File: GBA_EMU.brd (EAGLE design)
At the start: 130.7 x 72.9 mm, 99 parts, among them J1 USB-MINIB-5PIN, J2 AVR_SPI, SW1 LEFT, SW2 RIGHT, SW3 PWR_SWITCH, U1 MIC7221, U2 MCP1642B-ADJ, U4 LM4875, U5 Mic5365-2.8Y, U7 AZV321, X2 HEADPHONE

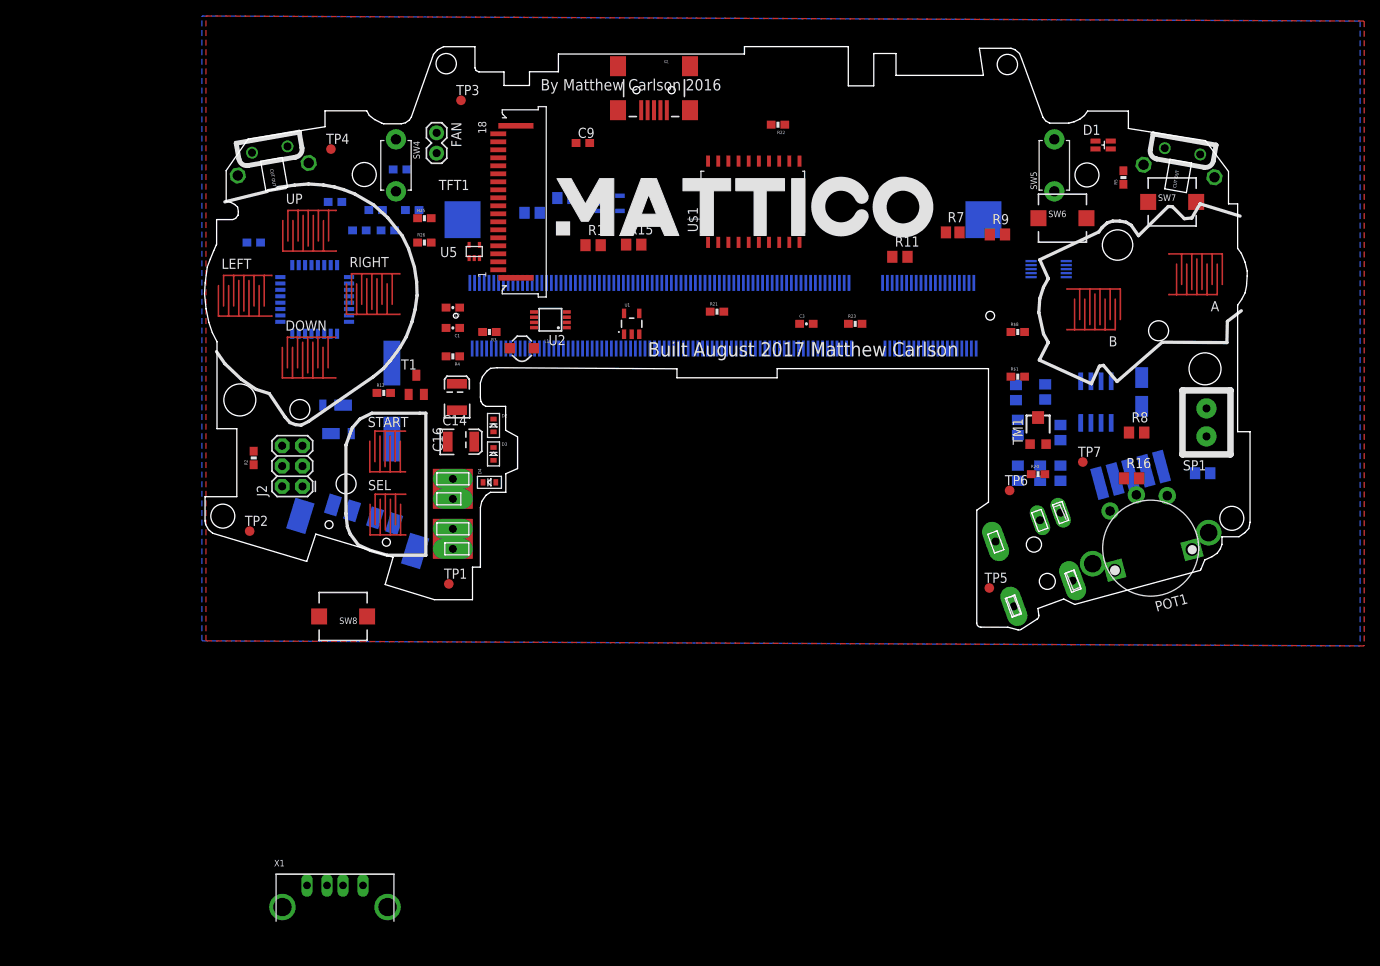
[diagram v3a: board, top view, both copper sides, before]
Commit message: moved connectors and whatnot
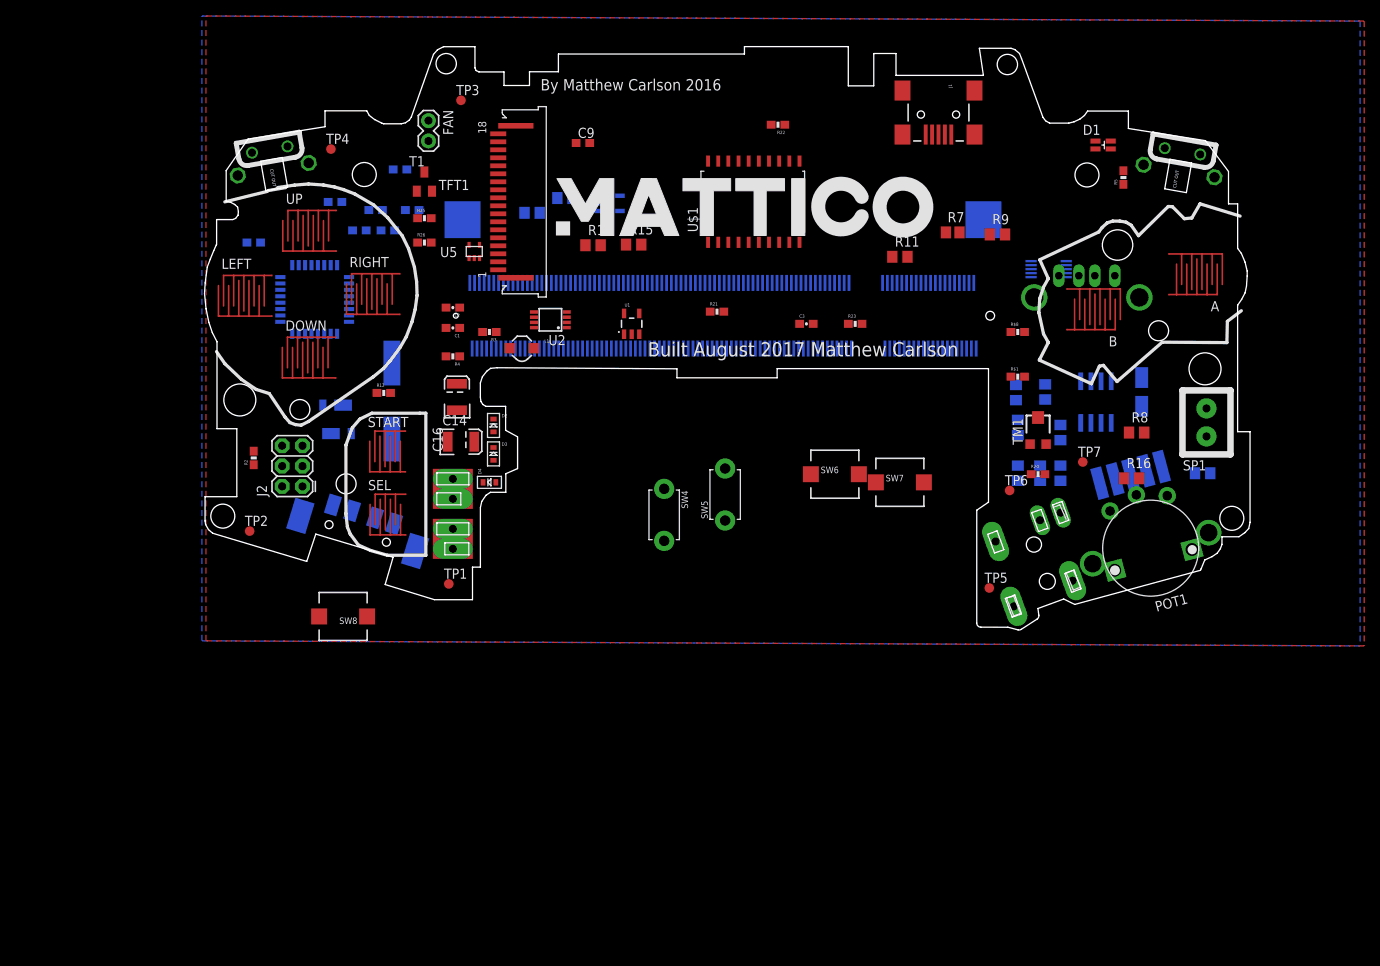
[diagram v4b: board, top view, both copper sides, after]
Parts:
- moved X1 121.0 mm to (131.6, 46.7), flipped to the bottom
- moved SW5 58.2 mm to (86.4, 25.9)
- moved SW4 55.1 mm to (78.7, 23.4)
- moved SW7 48.9 mm to (108.2, 27.4)
- moved SW6 42.8 mm to (100.1, 28.4)
- moved J1 35.7 mm to (113.0, 73.4)
- moved T1 25.4 mm to (48.8, 65.0)
- moved FAN 1.83 mm to (49.3, 72.6)
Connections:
- new net N$38: PCB1.47
- new net N$41: PCB1.23
- new net N$42: PCB1.27
- new net N$43: PCB1.29
- new net PI_SHUTDOWN: PCB1.69

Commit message: updated board render
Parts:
- moved SW5 49.9 mm to (99.1, 74.2)
- moved SW4 49.3 mm to (79.2, 72.6)
- moved SW7 21.3 mm to (112.8, 48.3)
- moved SW6 18.4 mm to (87.9, 42.2)
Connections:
- removed net N$38: PCB1.47
- net Y_BTN: now also PCB1.47
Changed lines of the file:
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@@
 <element name="U$1" library="custom" package="S020-75MM" value="CBT3244AD" x="84.224" y="62.512" rot="R90"/>
 <element name="POT1" library="adafruit" package="THUMBWHEEL" value="THUMBPOT" x="139.5508" y="19.2032" rot="R195"/>
-<element name="SW4" library="adafruit" package="TACT_PANA-EVQ" value="" x="78.74" y="23.368" rot="R270"/>
-<element name="SW5" library="adafruit" package="TACT_PANA-EVQ" value="" x="86.36" y="25.908" rot="R90"/>
+<element name="SW4" library="adafruit" package="TACT_PANA-EVQ" value="" x="79.248" y="72.644" rot="R270"/>
+<element name="SW5" library="adafruit" package="TACT_PANA-EVQ" value="" x="99.06" y="74.168" rot="R90"/>
 <element name="R13" library="SparkFun-Resistors" package="0603-RES" value="4.7K" x="45.72" y="66.548" rot="MR180">
 <attribute name="PROD_ID" value="RES-07857" x="45.72" y="66.548" size="1.778" layer="28" rot="MR180" display="off"/>
 </element>
-<element name="SW6" library="adafruit" package="PUSHBUTTON_SMD_SJ" value="" x="100.076" y="28.448"/>
-<element name="SW7" library="adafruit" package="PUSHBUTTON_SMD_SJ" value="" x="108.204" y="27.432"/>
+<element name="SW6" library="adafruit" package="PUSHBUTTON_SMD_SJ" value="" x="87.884" y="42.164"/>
+<element name="SW7" library="adafruit" package="PUSHBUTTON_SMD_SJ" value="" x="112.776" y="48.26"/>
 <element name="COPRO" library="adafruit" package="TQFP32-08" value="MEGA16u2" x="35.052" y="50.292" rot="MR0"/>
 <element name="R17" library="SparkFun-Resistors" package="0603-RES" value="22" x="37.592" y="62.484" rot="MR0">
@@
 <wire x1="106.94" y1="44.16" x2="108.74" y2="44.16" width="0" layer="19" extent="16-16"/>
 <wire x1="59.84" y1="52.36" x2="58.04" y2="52.36" width="0" layer="19" extent="16-16"/>
-<wire x1="55.64" y1="52.36" x2="58.04" y2="52.36" width="0" layer="19" extent="16-16"/>
-<wire x1="97.94" y1="44.16" x2="97.37" y2="47.244" width="0" layer="19" extent="1-16"/>
+<wire x1="85.34" y1="44.16" x2="84.884" y2="42.164" width="0" layer="19" extent="1-16"/>
+<wire x1="87.14" y1="44.16" x2="85.34" y2="44.16" width="0" layer="19" extent="16-16"/>
+<wire x1="88.94" y1="44.16" x2="87.14" y2="44.16" width="0" layer="19" extent="16-16"/>
+<wire x1="90.74" y1="44.16" x2="88.94" y2="44.16" width="0" layer="19" extent="16-16"/>
+<wire x1="92.54" y1="44.16" x2="90.74" y2="44.16" width="0" layer="19" extent="16-16"/>
+<wire x1="94.34" y1="44.16" x2="92.54" y2="44.16" width="0" layer="19" extent="16-16"/>
+<wire x1="96.14" y1="44.16" x2="94.34" y2="44.16" width="0" layer="19" extent="16-16"/>
+<wire x1="97.94" y1="44.16" x2="96.14" y2="44.16" width="0" layer="19" extent="16-16"/>
 <wire x1="99.74" y1="44.16" x2="97.94" y2="44.16" width="0" layer="19" extent="16-16"/>
 <wire x1="101.54" y1="44.16" x2="99.74" y2="44.16" width="0" layer="19" extent="16-16"/>
-<wire x1="96.14" y1="44.16" x2="97.94" y2="44.16" width="0" layer="19" extent="16-16"/>
-<wire x1="94.34" y1="44.16" x2="96.14" y2="44.16" width="0" layer="19" extent="16-16"/>
-<wire x1="92.54" y1="44.16" x2="94.34" y2="44.16" width="0" layer="19" extent="16-16"/>
-<wire x1="90.74" y1="44.16" x2="92.54" y2="44.16" width="0" layer="19" extent="16-16"/>
-<wire x1="88.94" y1="44.16" x2="90.74" y2="44.16" width="0" layer="19" extent="16-16"/>
-<wire x1="87.14" y1="44.16" x2="88.94" y2="44.16" width="0" layer="19" extent="16-16"/>
-<wire x1="85.34" y1="44.16" x2="87.14" y2="44.16" width="0" layer="19" extent="16-16"/>
 <wire x1="83.54" y1="44.16" x2="85.34" y2="44.16" width="0" layer="19" extent="16-16"/>
 <wire x1="81.74" y1="44.16" x2="83.54" y2="44.16" width="0" layer="19" extent="16-16"/>
@@
 <wire x1="65.54" y1="44.16" x2="67.34" y2="44.16" width="0" layer="19" extent="16-16"/>
 <wire x1="63.74" y1="44.16" x2="65.54" y2="44.16" width="0" layer="19" extent="16-16"/>
+<wire x1="55.64" y1="52.36" x2="58.04" y2="52.36" width="0" layer="19" extent="16-16"/>
 <wire x1="55" y1="55.46125" x2="55.64" y2="52.36" width="0" layer="19" extent="1-16"/>
 <wire x1="37.737625" y1="61.42204375" x2="39.79" y2="58.928" width="0" layer="19" extent="1-16"/>
@@
 <wire x1="52.324" y1="21.618" x2="46.42191875" y2="25.943271875" width="0" layer="19" extent="1-1"/>
 <wire x1="52.324" y1="19.118" x2="52.324" y2="21.618" width="0" layer="19" extent="1-1"/>
-<wire x1="86.36" y1="29.158" x2="87.14" y2="44.16" width="0" layer="19" extent="16-16"/>
 </signal>
 <signal name="TXD">
@@
 <contactref element="R26" pad="1"/>
 <contactref element="PCB1" pad="83"/>
-<wire x1="103.076" y1="28.448" x2="89.54" y2="44.16" width="0" layer="19" extent="1-16"/>
+<wire x1="90.884" y1="42.164" x2="89.54" y2="44.16" width="0" layer="19" extent="1-16"/>
 <wire x1="47.918" y1="57.404" x2="89.54" y2="44.16" width="0" layer="19" extent="1-16"/>
 </signal>
@@
 <contactref element="R25" pad="1"/>
 <contactref element="SW7" pad="P$1"/>
-<wire x1="47.918" y1="60.452" x2="111.204" y2="27.432" width="0" layer="19" extent="1-1"/>
+<contactref element="PCB1" pad="47"/>
+<wire x1="100.34" y1="44.16" x2="115.776" y2="48.26" width="0" layer="19" extent="1-16"/>
+<wire x1="47.918" y1="60.452" x2="100.34" y2="44.16" width="0" layer="19" extent="1-16"/>
 </signal>
 <signal name="L2_BTN">
@@
 <contactref element="SW4" pad="P$1"/>
 <contactref element="PCB1" pad="57"/>
-<wire x1="78.74" y1="26.618" x2="97.34" y2="44.16" width="0" layer="19" extent="16-16"/>
-<wire x1="27.432" y1="29.63" x2="78.74" y2="26.618" width="0" layer="19" extent="1-1"/>
+<wire x1="97.34" y1="44.16" x2="79.248" y2="75.894" width="0" layer="19" extent="16-16"/>
+<wire x1="27.432" y1="29.63" x2="79.248" y2="75.894" width="0" layer="19" extent="1-1"/>
 </signal>
 <signal name="R2_BTN">
@@
 <contactref element="SW5" pad="P$1"/>
 <contactref element="PCB1" pad="45"/>
-<wire x1="86.36" y1="22.658" x2="100.94" y2="44.16" width="0" layer="19" extent="16-16"/>
-<wire x1="44.87" y1="66.548" x2="100.94" y2="44.16" width="0" layer="19" extent="16-16"/>
+<wire x1="100.94" y1="44.16" x2="99.06" y2="70.918" width="0" layer="19" extent="16-16"/>
+<wire x1="44.87" y1="66.548" x2="99.06" y2="70.918" width="0" layer="19" extent="16-16"/>
 </signal>
 <signal name="COPRO_RX">
@@
 <contactref element="PCB1" pad="69"/>
 </signal>
-<signal name="N$38">
-<contactref element="PCB1" pad="47"/>
-</signal>
 <signal name="N$41">

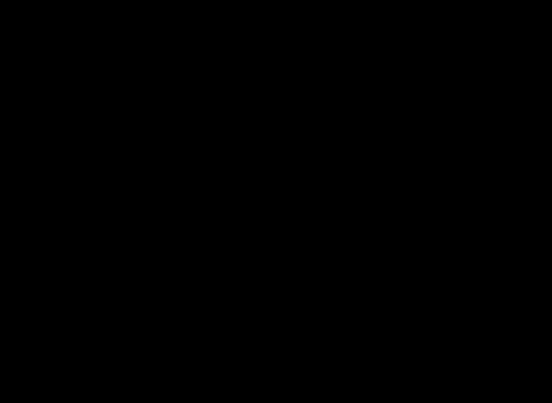
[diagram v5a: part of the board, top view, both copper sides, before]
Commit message: moved some labels around
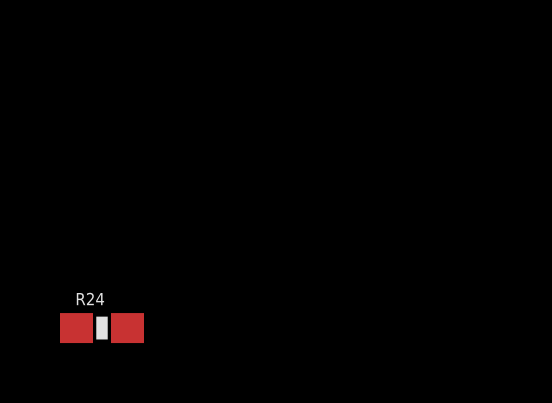
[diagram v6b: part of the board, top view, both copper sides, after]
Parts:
- added R24: 10K, SparkFun-Resistors:0603-RES
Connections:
- new net N$38: R24.2
- net PWR_EN: now also R24.1
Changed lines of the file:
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@@
 <element name="D6" library="custom" package="DIODE_POWERDI_123" value="" x="37.084" y="33.528" rot="MR180"/>
 <element name="X1" library="Adafruit_PowerBoost" package="MICROBUILDER_USB_HOST-PTH" value="" x="131.572" y="46.736" rot="MR0"/>
+<element name="R24" library="SparkFun-Resistors" package="0603-RES" value="10K" x="17.272" y="-10.16">
+<attribute name="PROD_ID" value="RES-00824" x="17.272" y="-10.16" size="1.778" layer="27" display="off"/>
+</element>
 </elements>
 <signals>
@@
 <contactref element="U2" pad="1"/>
 <contactref element="COPRO" pad="6"/>
+<contactref element="R24" pad="1"/>
 <wire x1="39.3446" y1="49.092" x2="66.566" y2="46.777" width="0" layer="19" extent="1-16"/>
+<wire x1="16.422" y1="-10.16" x2="39.3446" y2="49.092" width="0" layer="19" extent="1-16"/>
 </signal>
 <signal name="PI_SHUTDOWN">
@@
 <contactref element="PCB1" pad="29"/>
 </signal>
+<signal name="N$38">
+<contactref element="R24" pad="2"/>
+</signal>
 </signals>

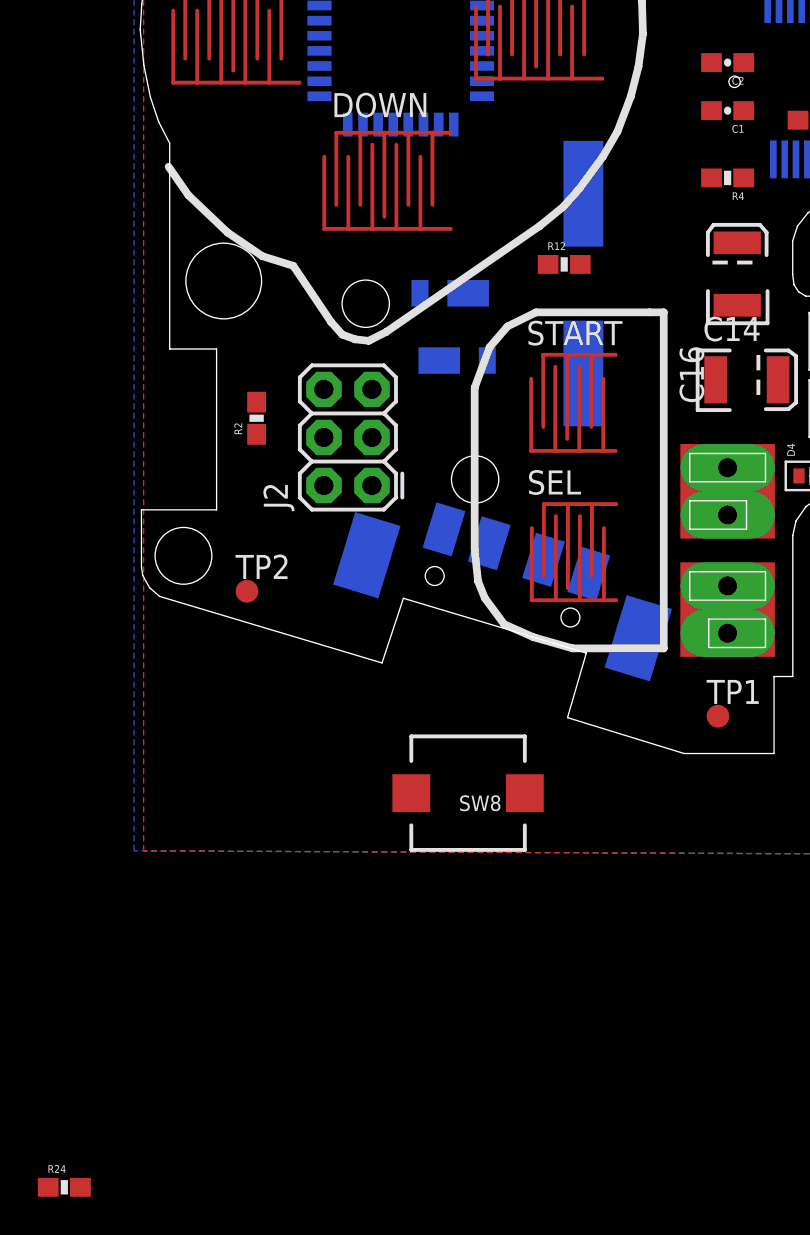
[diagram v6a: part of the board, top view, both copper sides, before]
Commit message: added power enable to Coprocessor
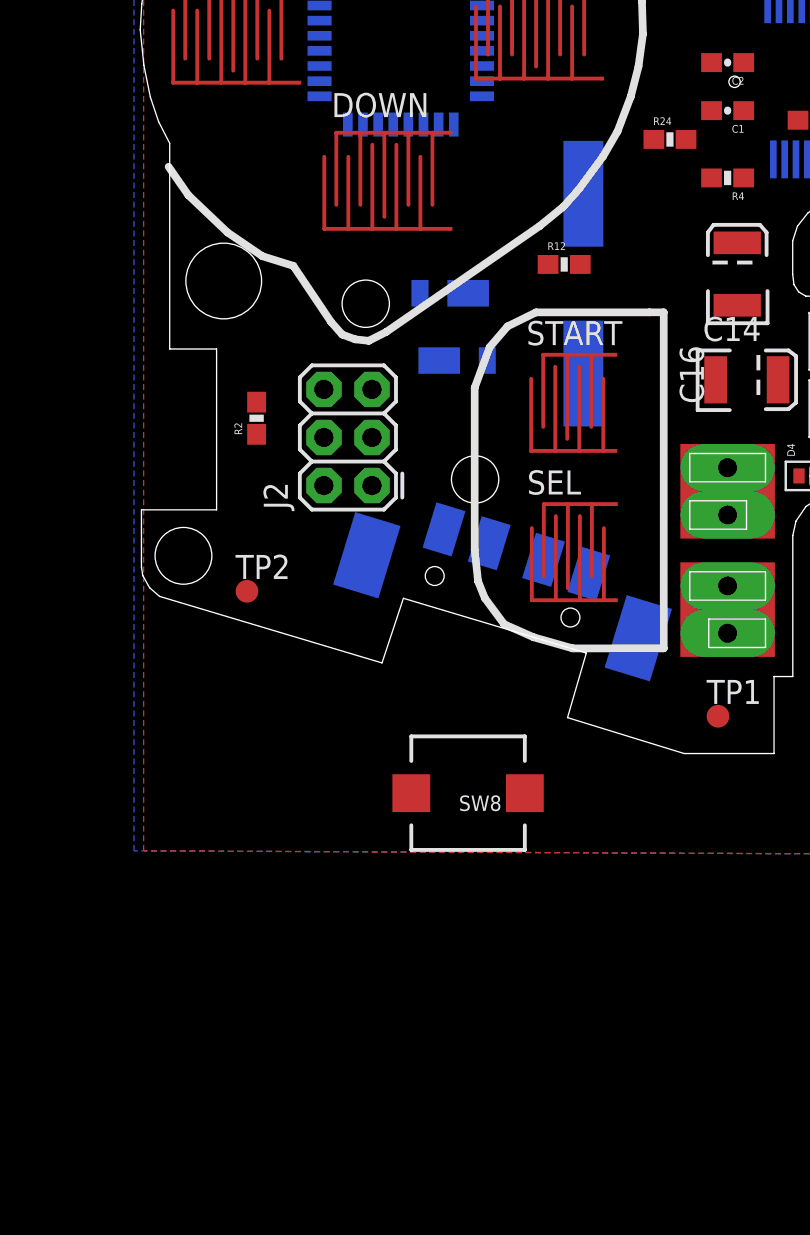
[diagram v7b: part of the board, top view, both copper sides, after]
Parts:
- moved R24 64.0 mm to (49.3, 45.2)
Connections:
- removed net N$38: R24.2
- new net N$44: COPRO.6, R24.1
- net GND: now also R23.1
- net PWR_EN: now also R23.2, R24.2; no longer COPRO.6, R24.1
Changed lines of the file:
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@@
 <element name="D6" library="custom" package="DIODE_POWERDI_123" value="" x="37.084" y="33.528" rot="MR180"/>
 <element name="X1" library="Adafruit_PowerBoost" package="MICROBUILDER_USB_HOST-PTH" value="" x="131.572" y="46.736" rot="MR0"/>
-<element name="R24" library="SparkFun-Resistors" package="0603-RES" value="10K" x="17.272" y="-10.16">
-<attribute name="PROD_ID" value="RES-00824" x="17.272" y="-10.16" size="1.778" layer="27" display="off"/>
+<element name="R24" library="SparkFun-Resistors" package="0603-RES" value="10K" x="49.276" y="45.212">
+<attribute name="PROD_ID" value="RES-00824" x="49.276" y="45.212" size="1.778" layer="27" display="off"/>
 </element>
 </elements>
@@
 <contactref element="C16" pad="C"/>
 <contactref element="X1" pad="GND"/>
+<contactref element="R23" pad="1"/>
 <wire x1="129" y1="54.584" x2="141.835725" y2="50.90233125" width="0" layer="19" extent="1-16"/>
 <wire x1="128.072" y1="53.256" x2="129" y2="54.584" width="0" layer="19" extent="16-16"/>
@@
 <wire x1="63.74" y1="44.16" x2="65.54" y2="44.16" width="0" layer="19" extent="16-16"/>
 <wire x1="55.64" y1="52.36" x2="58.04" y2="52.36" width="0" layer="19" extent="16-16"/>
+<wire x1="101.766" y1="47.244" x2="101.54" y2="44.16" width="0" layer="19" extent="1-16"/>
 <wire x1="55" y1="55.46125" x2="55.64" y2="52.36" width="0" layer="19" extent="1-16"/>
 <wire x1="37.737625" y1="61.42204375" x2="39.79" y2="58.928" width="0" layer="19" extent="1-16"/>
@@
 <signal name="PWR_EN">
 <contactref element="U2" pad="1"/>
+<contactref element="R23" pad="2"/>
+<contactref element="R24" pad="2"/>
+<wire x1="66.566" y1="46.777" x2="103.466" y2="47.244" width="0" layer="19" extent="1-1"/>
+<wire x1="50.126" y1="45.212" x2="66.566" y2="46.777" width="0" layer="19" extent="1-1"/>
+</signal>
+<signal name="PI_SHUTDOWN">
+<contactref element="PCB1" pad="69"/>
+</signal>
+<signal name="N$41">
+<contactref element="PCB1" pad="23"/>
+</signal>
+<signal name="N$42">
+<contactref element="PCB1" pad="27"/>
+</signal>
+<signal name="N$43">
+<contactref element="PCB1" pad="29"/>
+</signal>
+<signal name="N$44">
 <contactref element="COPRO" pad="6"/>
 <contactref element="R24" pad="1"/>
-<wire x1="39.3446" y1="49.092" x2="66.566" y2="46.777" width="0" layer="19" extent="1-16"/>
-<wire x1="16.422" y1="-10.16" x2="39.3446" y2="49.092" width="0" layer="19" extent="1-16"/>
-</signal>
-<signal name="PI_SHUTDOWN">
-<contactref element="PCB1" pad="69"/>
-</signal>
-<signal name="N$41">
-<contactref element="PCB1" pad="23"/>
-</signal>
-<signal name="N$42">
-<contactref element="PCB1" pad="27"/>
-</signal>
-<signal name="N$43">
-<contactref element="PCB1" pad="29"/>
-</signal>
-<signal name="N$38">
-<contactref element="R24" pad="2"/>
+<wire x1="39.3446" y1="49.092" x2="48.426" y2="45.212" width="0" layer="19" extent="1-16"/>
 </signal>
 </signals>
